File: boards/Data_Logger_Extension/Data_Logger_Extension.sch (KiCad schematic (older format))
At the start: 2 parts, among them J1 Ultrafit_5, J2 micromatch_female_RA_20

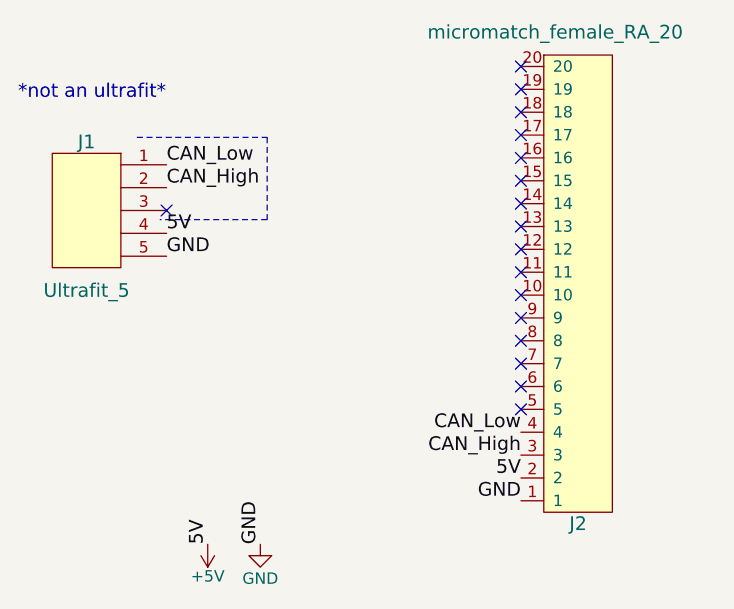
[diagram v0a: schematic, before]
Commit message: Fixed data logger.Can H/L
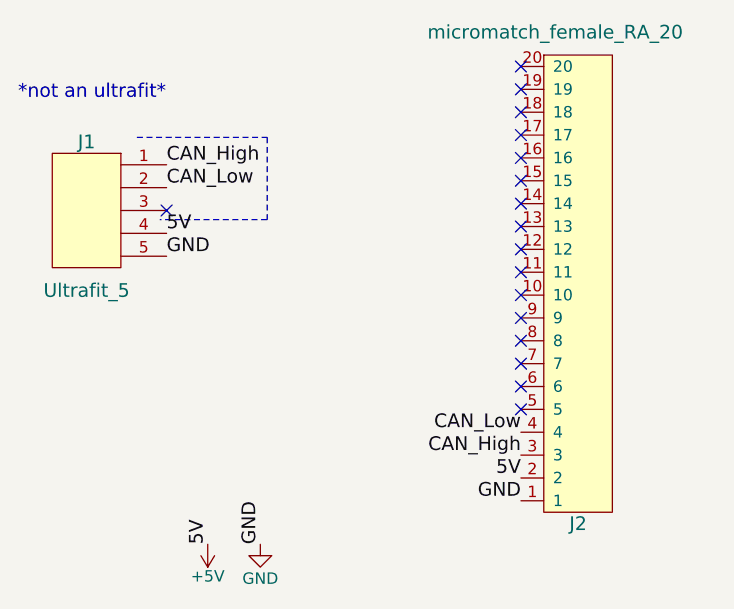
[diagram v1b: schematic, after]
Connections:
- net CAN_High: now also J1.1; no longer J1.2
- net CAN_Low: now also J1.2; no longer J1.1
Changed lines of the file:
@@
 LIBS:valves
 LIBS:formula
+LIBS:Data_Logger_Extension-cache
 EELAYER 25 0
 EELAYER END
@@
 Text Notes 730  850  0    60   ~ 0
 *not an ultrafit*
-Text Label 1380 1230 0    60   ~ 0
+Text Label 1380 1130 0    60   ~ 0
 CAN_High
-Text Label 1380 1130 0    60   ~ 0
-CAN_Low
 NoConn ~ 1380 1330
 Text Label 1380 1530 0    60   ~ 0
@@
 Text Label 1560 2790 1    60   ~ 0
 5V
+Text Label 1380 1230 0    60   ~ 0
+CAN_Low
 $EndSCHEMATC
